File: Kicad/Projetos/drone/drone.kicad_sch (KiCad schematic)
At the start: 19 parts, among them M1 Motor_Servo, M10 Motor_Servo, M11 Motor_Servo, M12 Motor_Servo, M13 Motor_Servo, M14 Motor_Servo, M15 Motor_Servo, M16 Motor_Servo, M17 Motor_Servo, M18 Motor_Servo, M2 Motor_Servo, M3 Motor_Servo, M4 Motor_Servo, M5 Motor_Servo, M6 Motor_Servo, M7 Motor_Servo, M8 Motor_Servo, M9 Motor_Servo, U3 DEVKIT_V1_ESP32-WROOM-32

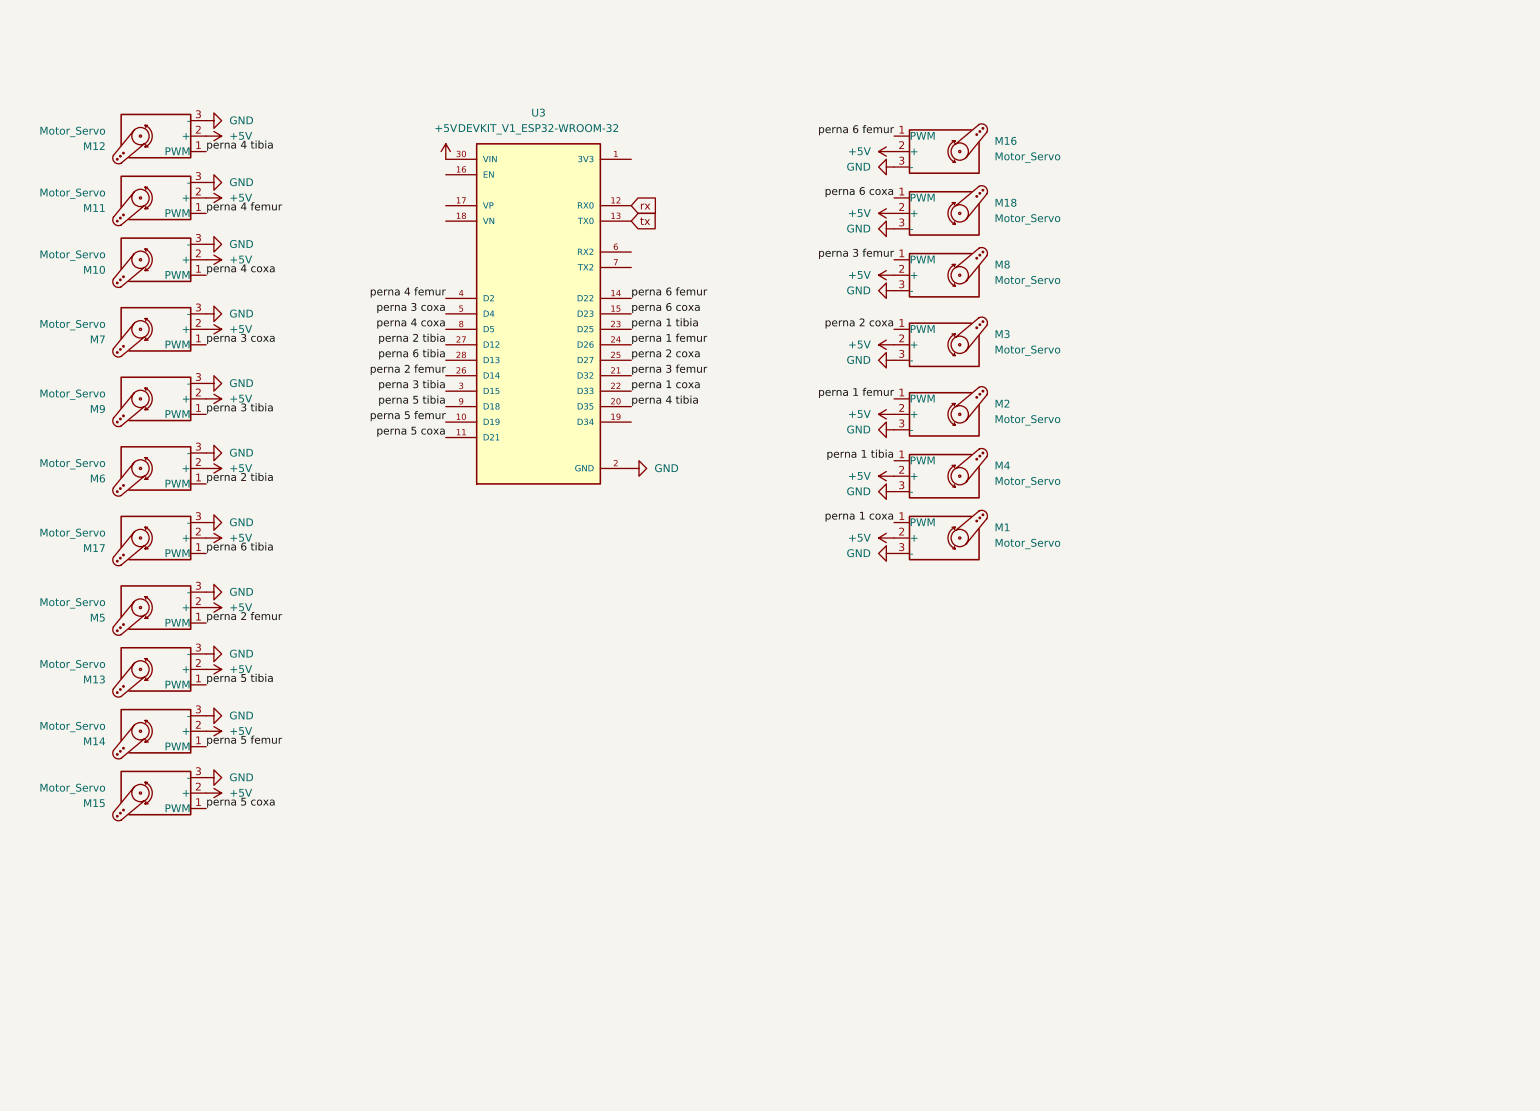
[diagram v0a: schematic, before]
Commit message: capacitores de desacoplamento no kicad
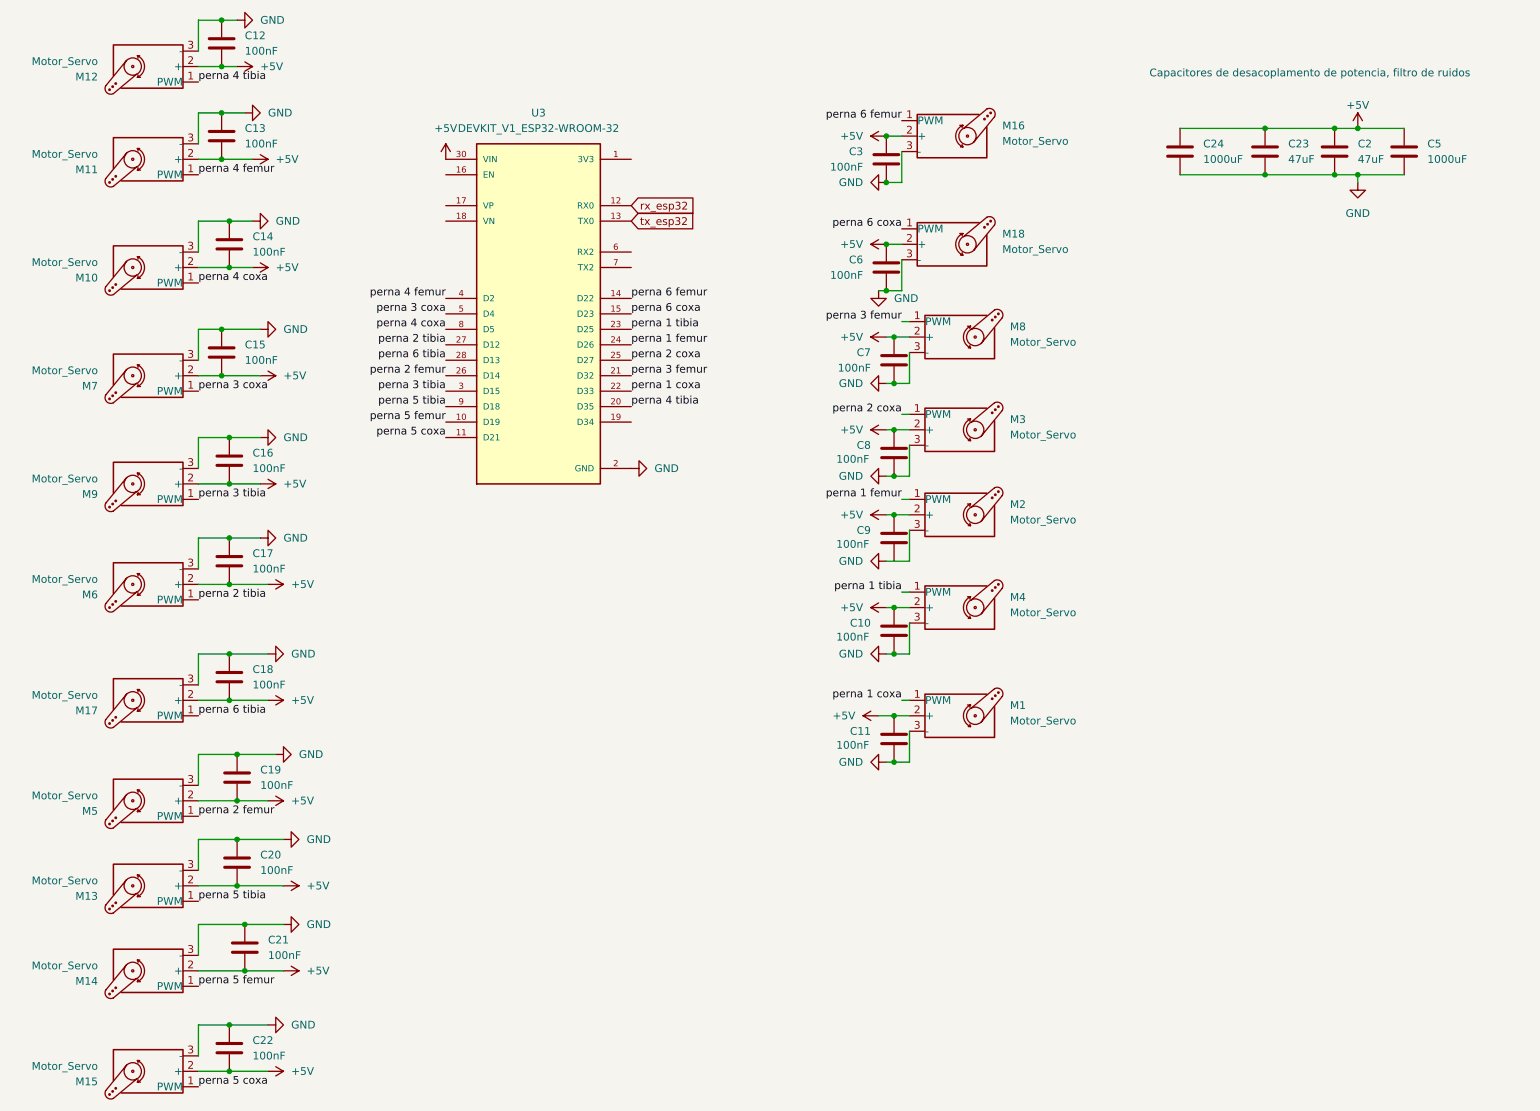
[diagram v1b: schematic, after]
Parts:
- added C10, C11, C12, C13, C14, C15, C16, C17, C18, C19, C20, C21, C22, C3, C6, C7, C8, C9: 100nF, Capacitor_THT:C_Disc_D7.0mm_W2.5mm_P5.00mm, symbol Device:C
- added C2, C23: 47uF, Capacitor_THT:C_Disc_D7.0mm_W2.5mm_P5.00mm, symbol Device:C
- added C24, C5: 1000uF, Capacitor_THT:C_Disc_D7.0mm_W2.5mm_P5.00mm, symbol Device:C
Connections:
- net +5V: now also C10.1, C11.1, C12.2, C13.2, C14.2, C15.2, C16.2, C17.2, C18.2, C19.2, C2.1, C20.2, C21.2, C22.2, C23.1, C24.1, C3.1, C5.1, C6.1, C7.1, C8.1, C9.1
- net GND: now also C10.2, C11.2, C12.1, C13.1, C14.1, C15.1, C16.1, C17.1, C18.1, C19.1, C2.2, C20.1, C21.1, C22.1, C23.2, C24.2, C3.2, C5.2, C6.2, C7.2, C8.2
- net rx renamed rx_esp32
- net tx renamed tx_esp32
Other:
- note added: "Capacitores de desacoplamento de potencia, filtro de ruidos"
- moved on the sheet: M1, M10, M11, M12, M13, M14, M15, M16, M17, M18, M2, M3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
